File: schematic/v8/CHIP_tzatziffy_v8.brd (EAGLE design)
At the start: 40.9 x 49.8 mm, 61 parts, among them J1 2X20-CHIP0.8_DRILL_0.15OFFSET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, Q2 n.a. / 2N7002ET1G, U1 n.a. / LMR62421, U3 DS2431P, X1 FH12-40S-0.5SH

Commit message: use of new usb lib
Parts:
- removed USB: USBUSB-MICROB-SMT-DIP, Spark:USB-MICROB-SMT-DIP
- added JP1: USBUSB-MICROB-SMT-DIP, JKW_CHIP:USB-MICROB-SMT-DIP
- added JP2: USBMICRO_SMD, JKW_CHIP:USB-B-MICRO-SMD_V03
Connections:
- net GND: now also JP1.GND, JP1.MT1, JP1.MT2, JP1.MT3, JP1.MT4, JP1.P$1, JP1.P$2, JP2.GND, JP2.SHIELD1, JP2.SHIELD2, JP2.SHIELD3; no longer USB.GND, USB.MT1, USB.MT2
- net VOUT: now also JP1.VBUS, JP2.VBUS; no longer USB.VBUS
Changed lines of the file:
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@@
 <attribute name="VALUE" x="34.655" y="19.05" size="1.27" layer="27" rot="R180"/>
-</element>
-<element name="USB" library="Spark" package="USB-MICROB-SMT-DIP" value="USBUSB-MICROB-SMT-DIP" x="11.75" y="48.375" smashed="yes" rot="R180">
-<attribute name="NAME" x="15.425" y="47.225" size="0.8128" layer="25" font="vector" rot="R270"/>
-<attribute name="VALUE" x="13.655" y="51.65" size="0.762" layer="27" rot="R180"/>
 </element>
 <element name="SJ4" library="JKW_CHIP" package="SMD_SJ_3WAY_OPEN" value="" x="27.75" y="33.125" smashed="yes" rot="MR270">
@@
 <attribute name="VALUE" x="31.12" y="20.71" size="1.27" layer="28" rot="MR0"/>
 </element>
+<element name="JP1" library="JKW_CHIP" package="USB-MICROB-SMT-DIP" value="USBUSB-MICROB-SMT-DIP" x="11.75" y="48.375" rot="R180"/>
+<element name="JP2" library="JKW_CHIP" package="USB-B-MICRO-SMD_V03" value="USBMICRO_SMD" x="-3.6" y="4.5"/>
 </elements>
 <signals>
@@
 <wire x1="35.543" y1="49.082" x2="36.905" y2="49.082" width="0.3048" layer="16"/>
 <via x="28.119" y="46.818" extent="1-16" drill="0.3048"/>
-<contactref element="USB" pad="GND"/>
-<contactref element="USB" pad="MT2"/>
-<contactref element="USB" pad="MT1"/>
 <contactref element="U$10" pad="GNDOUT"/>
 <contactref element="U$10" pad="GNDIN"/>
@@
 <wire x1="30.8" y1="23.25" x2="30.825" y2="23.275" width="0.254" layer="16"/>
 <wire x1="30.825" y1="23.275" x2="30.825" y2="25.125" width="0.254" layer="16"/>
+<contactref element="JP1" pad="MT2"/>
+<contactref element="JP1" pad="MT1"/>
+<contactref element="JP1" pad="GND"/>
+<contactref element="JP1" pad="P$1"/>
+<contactref element="JP1" pad="MT4"/>
+<contactref element="JP1" pad="P$2"/>
+<contactref element="JP1" pad="MT3"/>
+<contactref element="JP2" pad="SHIELD3"/>
+<contactref element="JP2" pad="SHIELD1"/>
+<contactref element="JP2" pad="GND"/>
+<contactref element="JP2" pad="SHIELD2"/>
+<wire x1="-3.6" y1="4.5" x2="-3.6" y2="8.185" width="0" layer="19" extent="1-1"/>
+<wire x1="-0.875" y1="3.2" x2="-3.6" y2="4.5" width="0" layer="19" extent="1-1"/>
+<wire x1="1.195" y1="0.822" x2="-0.875" y2="3.2" width="0" layer="19" extent="1-1"/>
+<wire x1="-3.6" y1="0.815" x2="-0.875" y2="3.2" width="0" layer="19" extent="1-1"/>
 </signal>
 <signal name="VREG_OUTPUT">
@@
 </signal>
 <signal name="VOUT">
-<contactref element="USB" pad="VBUS"/>
 <contactref element="J1" pad="CHG-IN"/>
 <contactref element="SJ4" pad="1"/>
@@
 <wire x1="8.875" y1="39.875" x2="5.875" y2="42.875" width="0.3048" layer="16"/>
 <via x="5.875" y="42.875" extent="1-16" drill="0.3048"/>
-<wire x1="13.05" y1="45.7" x2="13.05" y2="44.925" width="0.3048" layer="1"/>
-<wire x1="13.05" y1="44.925" x2="12.625" y2="44.5" width="0.3048" layer="1"/>
+<wire x1="12.9" y1="44.775" x2="12.625" y2="44.5" width="0.3048" layer="1"/>
 <wire x1="12.625" y1="44.5" x2="5.875" y2="44.5" width="0.3048" layer="1"/>
 <wire x1="8.875" y1="39.875" x2="24.875" y2="39.875" width="0.3048" layer="16"/>
@@
 <wire x1="5.875" y1="47.017" x2="3.81" y2="49.082" width="0.3048" layer="1"/>
 <wire x1="3.81" y1="49.082" x2="3.735" y2="49.082" width="0.3048" layer="1"/>
+<contactref element="JP1" pad="VBUS"/>
+<wire x1="13.05" y1="45.7" x2="13.05" y2="44.925" width="0.3048" layer="1"/>
+<wire x1="13.05" y1="44.925" x2="12.9" y2="44.775" width="0.3048" layer="1"/>
+<contactref element="JP2" pad="VBUS"/>
+<wire x1="-0.875" y1="5.8" x2="8.875" y2="39.875" width="0" layer="19" extent="1-16"/>
 </signal>
 <signal name="PWR_IN">

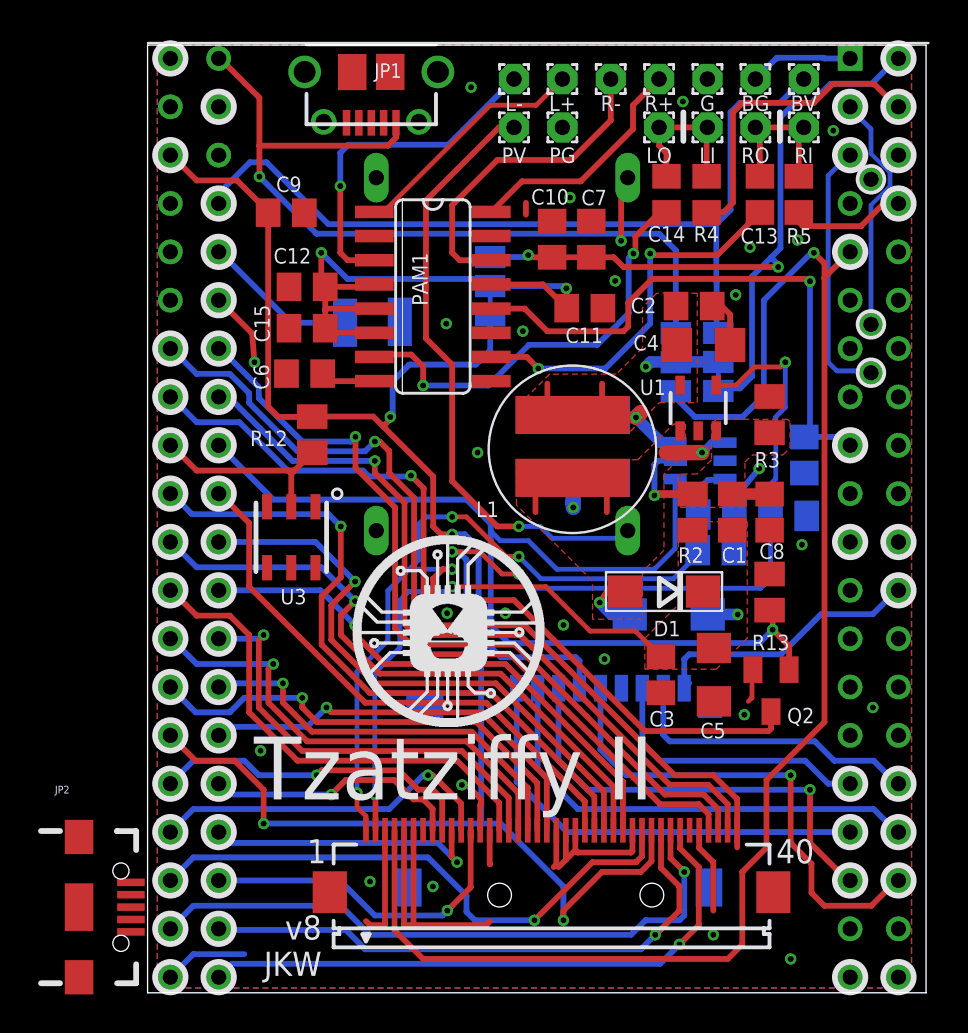
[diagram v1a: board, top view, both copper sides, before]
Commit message: added new smd usb
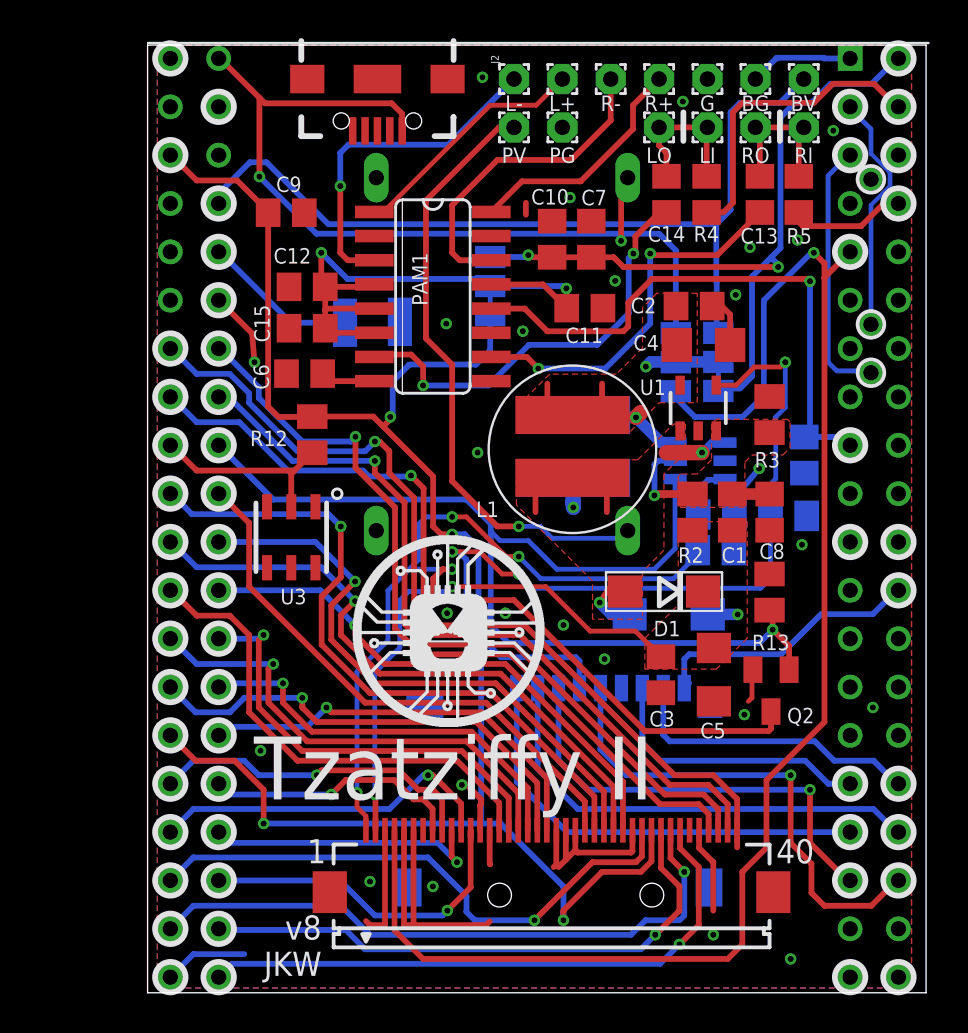
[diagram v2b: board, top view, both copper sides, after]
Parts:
- removed JP1: USBUSB-MICROB-SMT-DIP, JKW_CHIP:USB-MICROB-SMT-DIP
- removed JP2: USBMICRO_SMD, JKW_CHIP:USB-B-MICRO-SMD_V03
- added J2: USB-MICROB", JKW_CHIP:USB-B-MICRO-SMD_V03
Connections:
- net GND: now also J2.GND, J2.SHIELD1, J2.SHIELD2, J2.SHIELD3; no longer JP1.GND, JP1.MT1, JP1.MT2, JP1.MT3, JP1.MT4, JP1.P$1, JP1.P$2, JP2.GND, JP2.SHIELD1, JP2.SHIELD2, JP2.SHIELD3
- net VOUT: now also J2.VBUS; no longer JP1.VBUS, JP2.VBUS
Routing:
- net VOUT: track 46.9 -> 47.6 mm
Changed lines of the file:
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@@
 <?xml version="1.0" encoding="utf-8"?>
 <!DOCTYPE eagle SYSTEM "eagle.dtd">
-<eagle version="7.6.0">
+<eagle version="7.7.0">
 <drawing>
 <settings>
@@
 <attribute name="VALUE" x="31.12" y="20.71" size="1.27" layer="28" rot="MR0"/>
 </element>
-<element name="JP1" library="JKW_CHIP" package="USB-MICROB-SMT-DIP" value="USBUSB-MICROB-SMT-DIP" x="11.75" y="48.375" rot="R180"/>
-<element name="JP2" library="JKW_CHIP" package="USB-B-MICRO-SMD_V03" value="USBMICRO_SMD" x="-3.6" y="4.5"/>
+<element name="J2" library="JKW_CHIP" package="USB-B-MICRO-SMD_V03" value="USB-MICROB&quot;" x="12.075" y="48" rot="R270">
+<attribute name="PROD_ID" value="CONN-11752" x="12.075" y="48" size="1.778" layer="27" rot="R270" display="off"/>
+</element>
 </elements>
 <signals>
@@
 <via x="24.565" y="37.398" extent="1-16" drill="0.3048"/>
 <via x="17.336" y="28.379" extent="1-16" drill="0.3048"/>
-<via x="16.994" y="47.568" extent="1-16" drill="0.3048"/>
+<via x="17.594" y="48.093" extent="1-16" drill="0.3048"/>
 <wire x1="11.9126" y1="39.751" x2="12.0396" y2="39.878" width="0.3048" layer="1"/>
 <via x="21.844" y="19.32" extent="1-16" drill="0.3048"/>
@@
 <wire x1="30.8" y1="23.25" x2="30.825" y2="23.275" width="0.254" layer="16"/>
 <wire x1="30.825" y1="23.275" x2="30.825" y2="25.125" width="0.254" layer="16"/>
-<contactref element="JP1" pad="MT2"/>
-<contactref element="JP1" pad="MT1"/>
-<contactref element="JP1" pad="GND"/>
-<contactref element="JP1" pad="P$1"/>
-<contactref element="JP1" pad="MT4"/>
-<contactref element="JP1" pad="P$2"/>
-<contactref element="JP1" pad="MT3"/>
-<contactref element="JP2" pad="SHIELD3"/>
-<contactref element="JP2" pad="SHIELD1"/>
-<contactref element="JP2" pad="GND"/>
-<contactref element="JP2" pad="SHIELD2"/>
-<wire x1="-3.6" y1="4.5" x2="-3.6" y2="8.185" width="0" layer="19" extent="1-1"/>
-<wire x1="-0.875" y1="3.2" x2="-3.6" y2="4.5" width="0" layer="19" extent="1-1"/>
-<wire x1="1.195" y1="0.822" x2="-0.875" y2="3.2" width="0" layer="19" extent="1-1"/>
-<wire x1="-3.6" y1="0.815" x2="-0.875" y2="3.2" width="0" layer="19" extent="1-1"/>
+<contactref element="J2" pad="GND"/>
+<contactref element="J2" pad="SHIELD1"/>
+<contactref element="J2" pad="SHIELD2"/>
+<contactref element="J2" pad="SHIELD3"/>
 </signal>
 <signal name="VREG_OUTPUT">
@@
 <wire x1="8.875" y1="39.875" x2="5.875" y2="42.875" width="0.3048" layer="16"/>
 <via x="5.875" y="42.875" extent="1-16" drill="0.3048"/>
-<wire x1="12.9" y1="44.775" x2="12.625" y2="44.5" width="0.3048" layer="1"/>
-<wire x1="12.625" y1="44.5" x2="5.875" y2="44.5" width="0.3048" layer="1"/>
 <wire x1="8.875" y1="39.875" x2="24.875" y2="39.875" width="0.3048" layer="16"/>
 <wire x1="24.875" y1="39.875" x2="26.875" y2="39.875" width="0.3048" layer="16"/>
 <via x="24.875" y="39.5" extent="1-16" drill="0.3048"/>
 <contactref element="U$10" pad="VOUT"/>
-<wire x1="5.875" y1="44.5" x2="5.875" y2="47.017" width="0.3048" layer="1"/>
-<wire x1="5.875" y1="42.875" x2="5.875" y2="44.5" width="0.3048" layer="1"/>
+<wire x1="5.875" y1="42.875" x2="5.875" y2="47.017" width="0.3048" layer="1"/>
 <wire x1="24.875" y1="39.5" x2="24.875" y2="42.473" width="0.3048" layer="1"/>
 <wire x1="24.875" y1="42.473" x2="25.222" y2="42.82" width="0.3048" layer="1"/>
 <wire x1="24.875" y1="39.5" x2="24.875" y2="39.875" width="0.3048" layer="16"/>
-<wire x1="5.875" y1="47.017" x2="3.81" y2="49.082" width="0.3048" layer="1"/>
+<wire x1="5.875" y1="47.017" x2="5.446" y2="47.446" width="0.3048" layer="1"/>
+<wire x1="5.446" y1="47.446" x2="3.81" y2="49.082" width="0.3048" layer="1"/>
 <wire x1="3.81" y1="49.082" x2="3.735" y2="49.082" width="0.3048" layer="1"/>
-<contactref element="JP1" pad="VBUS"/>
-<wire x1="13.05" y1="45.7" x2="13.05" y2="44.925" width="0.3048" layer="1"/>
-<wire x1="13.05" y1="44.925" x2="12.9" y2="44.775" width="0.3048" layer="1"/>
-<contactref element="JP2" pad="VBUS"/>
-<wire x1="-0.875" y1="5.8" x2="8.875" y2="39.875" width="0" layer="19" extent="1-16"/>
+<contactref element="J2" pad="VBUS"/>
+<wire x1="13.375" y1="45.275" x2="13.375" y2="46.175" width="0.3048" layer="1"/>
+<wire x1="13.375" y1="46.175" x2="12.825" y2="46.725" width="0.3048" layer="1"/>
+<wire x1="12.825" y1="46.725" x2="6.167" y2="46.725" width="0.3048" layer="1"/>
+<wire x1="6.167" y1="46.725" x2="5.875" y2="47.017" width="0.3048" layer="1"/>
 </signal>
 <signal name="PWR_IN">
